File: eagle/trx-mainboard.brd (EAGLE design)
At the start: 94.8 x 82.9 mm, 0 parts

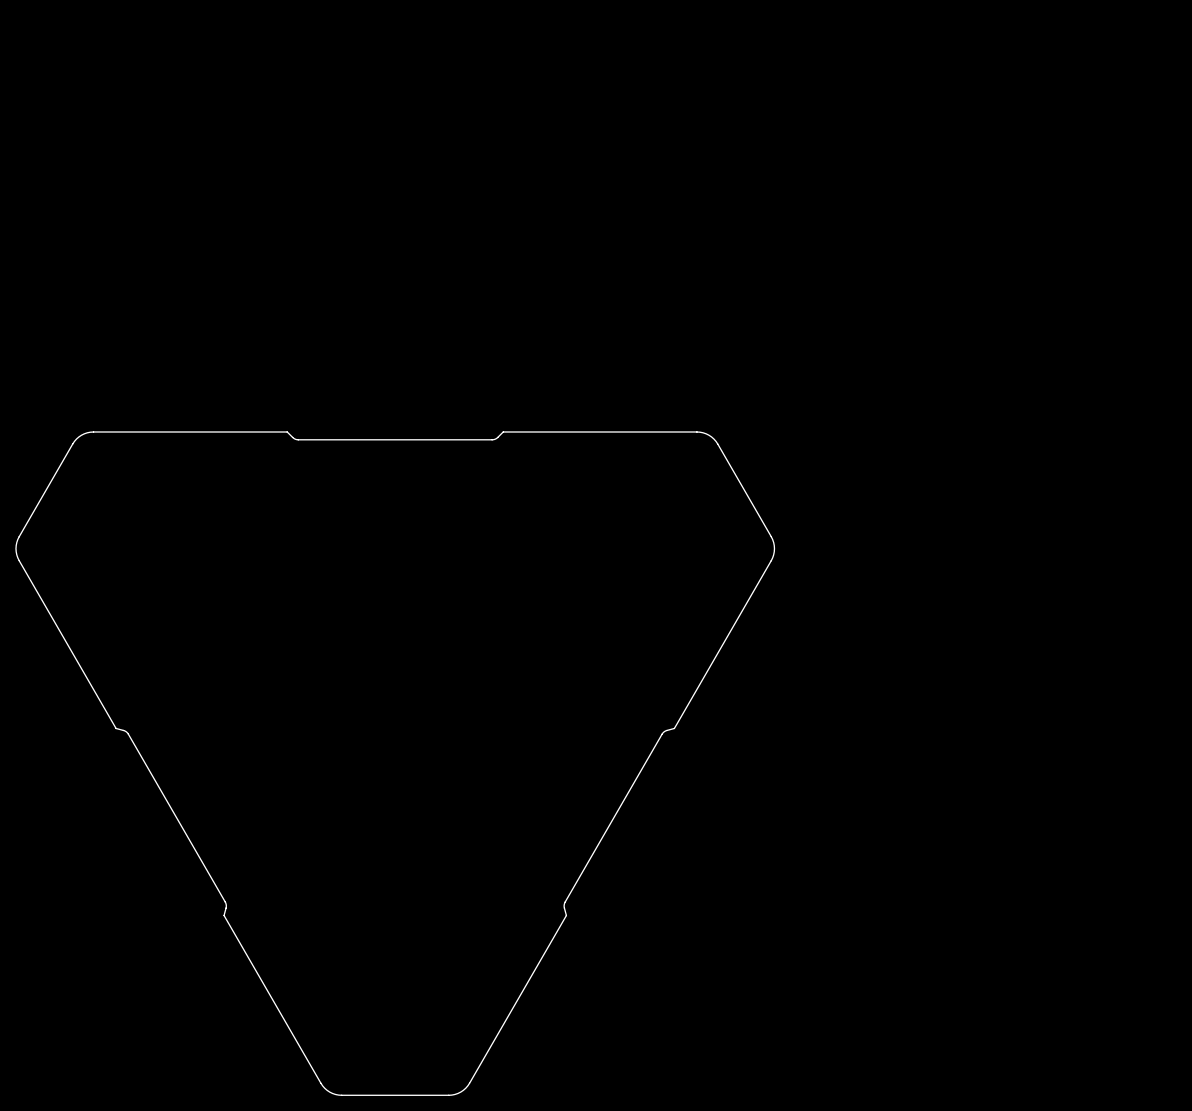
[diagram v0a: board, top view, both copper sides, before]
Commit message: Added eagle files and gitignore
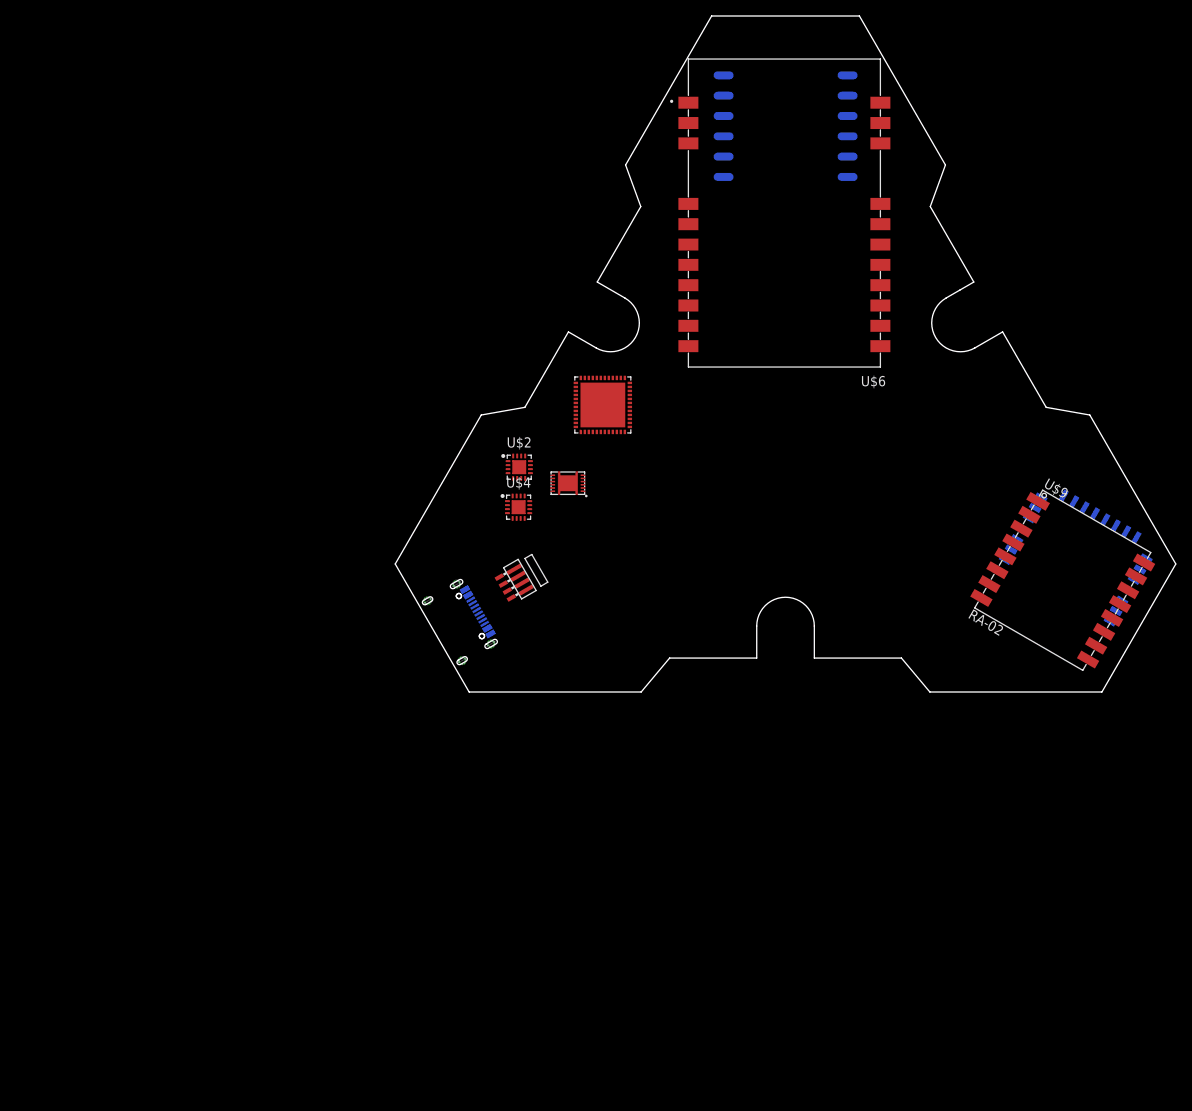
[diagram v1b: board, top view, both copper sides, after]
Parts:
- added J1: 629722000214, Wurth_Connectors_WR-USB:629722000214
- added U$1: L86-M33, quectel:L86-M33
- added U$10: STM32-F042X4/6-48, st-microelectronics:UFQFPN48-7X7
- added U$2: TPS6214X, texas-instruments:VQFN16-3X3
- added U$3: BQ27441, texas-instruments:SON12
- added U$4: BQ2407X, texas-instruments:VQFN16-3X3
- added U$5: JDY-23, bluetooth:JDY-23
- added U$6: E22-900M30S, ebyte:E22-900M30S
- added U$7: BC034-04-A-V-0150-L-C, con-gct:P-1X4/90-1.00X1.50MM-SMT
- added U$8: BC075-04-A-L-A, con-gct:S-1X4/90-1.00MM-SMT
- added U$9: RA-02, ai-thinker:RA-01/RA-02
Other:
- board size 94.8 x 82.9 mm -> 97.6 x 84.5 mm

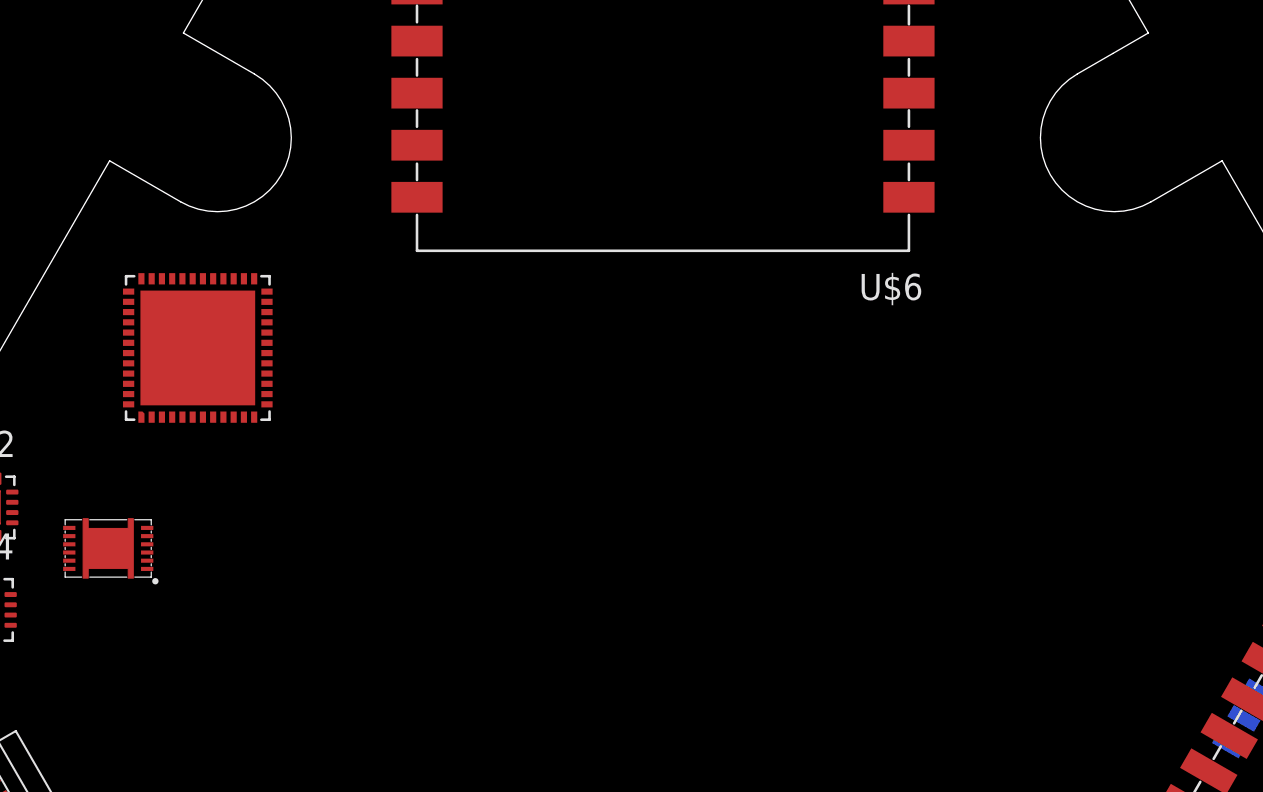
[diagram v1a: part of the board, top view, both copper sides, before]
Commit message: Added display pinheader
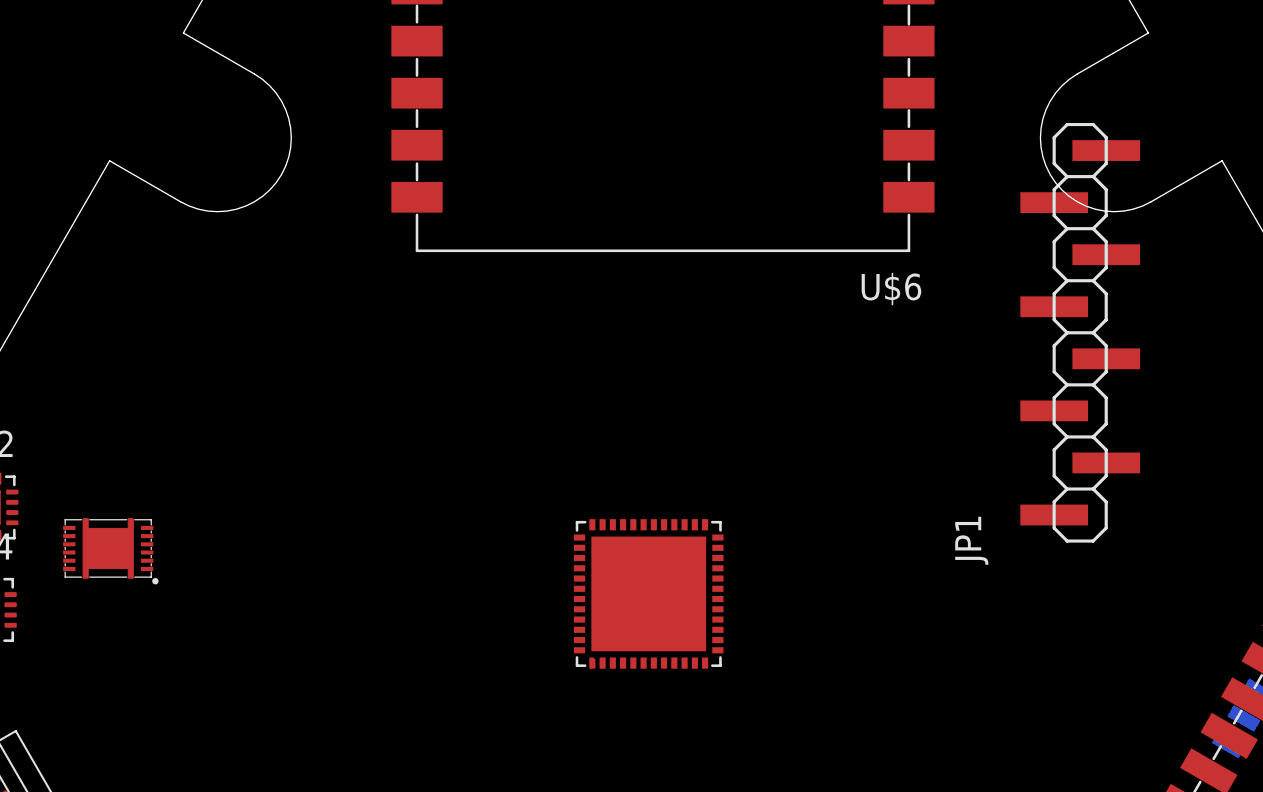
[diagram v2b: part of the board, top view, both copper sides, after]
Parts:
- added JP1: (no value), pinhead2:1X08SMD
- moved U$10 25.1 mm to (48.0, 23.9)
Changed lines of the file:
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@@
 </layers>
 <board>
+<fusionsync huburn="a.cGVyc29uYWw6dWUyZDQ3YTFj" projecturn="a.cGVyc29uYWw6dWUyZDQ3YTFjIzIwMTkxMDEyMjI1OTkyMjA2" f3durn="urn:adsk.wipprod:dm.lineage:G3ybIRbiT7ecl5LWR0nKqA" pcbguid="" lastpulledtime="" lastsyncedchangeguid="" latestrevisionid="6f82d806-30c5-4c96-a74c-11b18f3c1102" lastsyncedrevisionid="6f82d806-30c5-4c96-a74c-11b18f3c1102" lastboardhashguid="7c8f62d4-8a94-028a-21ff-13d31bc08e46" lastpushedtime="2023-05-01T20:54:56Z" linktopcb3d="true"/>
 <plain>
 <dimension x1="48" y1="40" x2="49" y2="5" x3="111.0774875" y3="24.287928125" textsize="1.778" layer="16"/>
@@
 <attribute name="VALUE" x="71.511796875" y="9.309734375" size="1.27" layer="21" rot="R330"/>
 </element>
-<element name="U$10" library="st-microelectronics" library_urn="urn:adsk.eagle:library:18661622" package="UFQFPN48-7X7" package3d_urn="urn:adsk.eagle:package:18661624/3" value="STM32-F042X4/6-48" x="25.95" y="35.88" smashed="yes" rot="R90"/>
+<element name="U$10" library="st-microelectronics" library_urn="urn:adsk.eagle:library:18661622" package="UFQFPN48-7X7" package3d_urn="urn:adsk.eagle:package:18661624/3" value="STM32-F042X4/6-48" x="47.95" y="23.88" smashed="yes" rot="R90"/>
+<element name="JP1" library="pinhead2" library_urn="urn:adsk.eagle:library:40219860" package="1X08SMD" package3d_urn="urn:adsk.eagle:package:40220540/2" value="" x="69" y="29" smashed="yes" rot="R90">
+<attribute name="NAME" x="64.1712" y="25.3838" size="1.27" layer="25" ratio="10" rot="R90"/>
+<attribute name="VALUE" x="72.175" y="26.46" size="1.27" layer="27" rot="R90"/>
+</element>
 </elements>
 <signals>
@@
 </note>
 <note version="8.3" severity="warning">
+Since Version 8.3, EAGLE supports Fusion synchronisation.
+This feature will not be available in this version and saving
+the document will break the link to the Fusion PCB feature.
+</note>
+<note version="8.3" severity="warning">

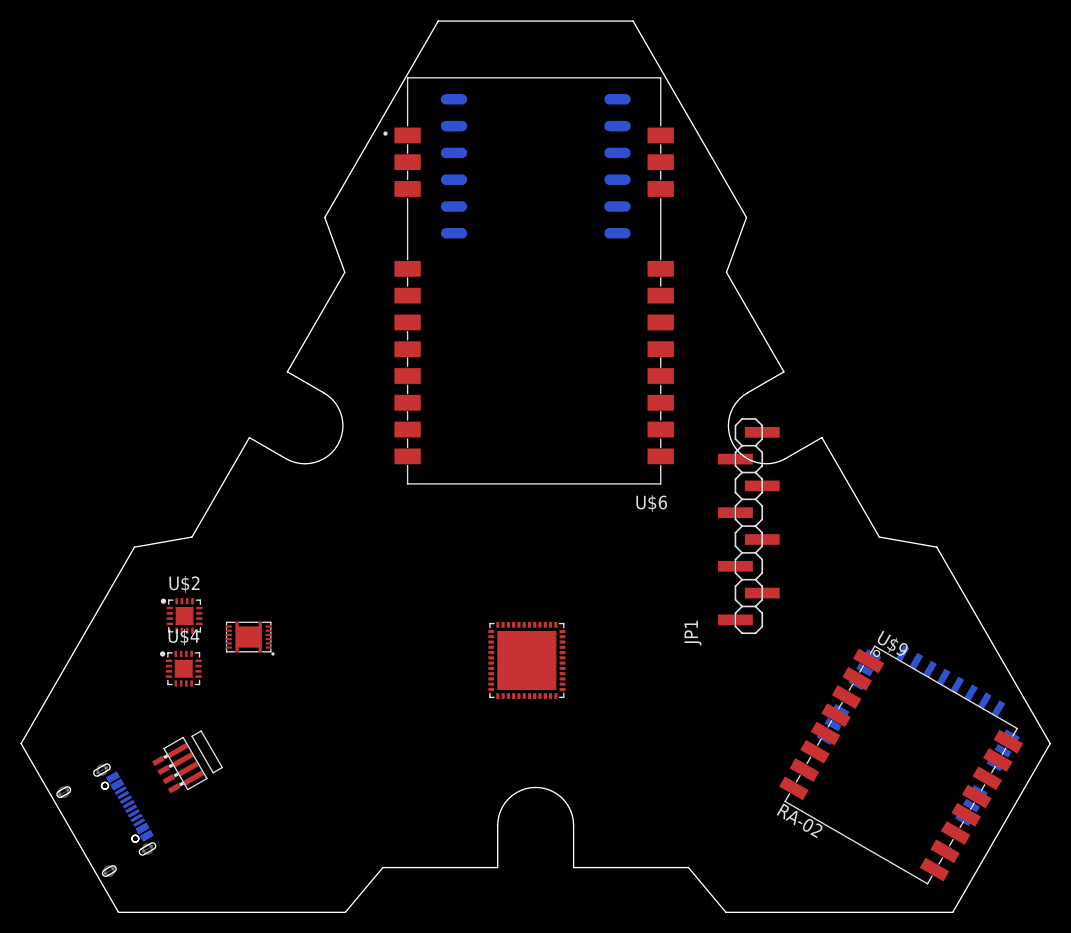
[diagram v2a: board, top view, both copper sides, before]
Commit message: Changed board layout
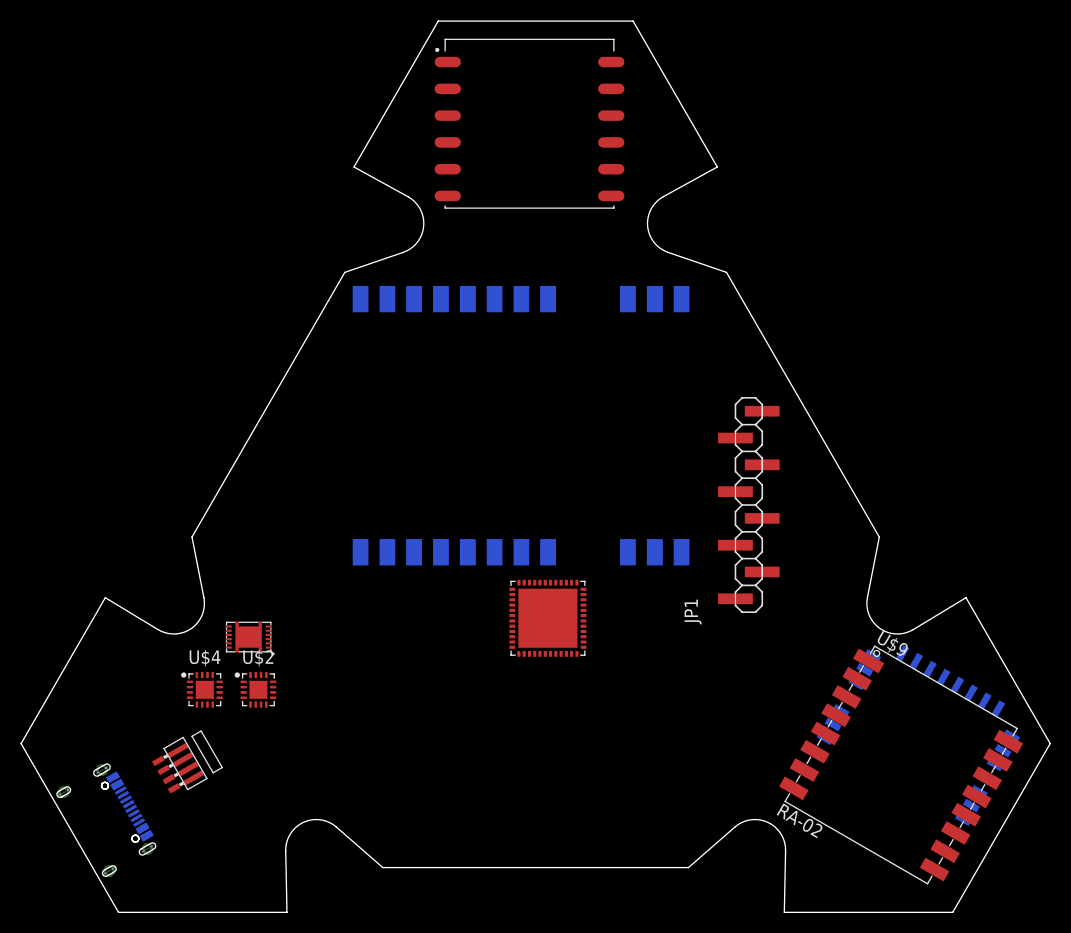
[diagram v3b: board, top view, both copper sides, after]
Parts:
- moved U$6 13.7 mm to (48.8, 46.1), flipped to the bottom, turned to 270 degrees
- moved U$2 9.90 mm to (22.5, 21.1)
- moved U$10 4.47 mm to (50.0, 27.9)
- moved U$1 3.58 mm to (48.2, 74.3), flipped to the top, turned to 0 degrees
- moved U$4 2.83 mm to (17.4, 21.1)
- moved JP1 2.00 mm to (69.0, 31.0)
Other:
- outline, holes or cut-outs redrawn

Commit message: Added further components to pcb
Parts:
- added C1, C11, C12, C13, C2, C3: 100nF, rcl:C0805
- added C10, C4, C5, C6, C8: 4.7uF, rcl:C0805
- added C7: 1uF, rcl:C0805
- added C9: (no value), rcl:PANASONIC_C
- added R1, R2: 5.1k, rcl:R0805
- added R3, R4, R5, R6: 3k, rcl:R0805
- U$3: value BQ27441 -> BQ2407X; device texas-instruments:SON12 -> texas-instruments:VQFN16-3X3
- U$4: value BQ2407X -> IHLP-1212; device texas-instruments:VQFN16-3X3 -> inductor-vishay:1212BZ
- U$6: value E22-900M30S -> E32-900M30S; device ebyte:E22-900M30S -> ebyte:E32-900M30S
- moved U$2 6.92 mm to (22.0, 28.0)
- moved U$3 4.89 mm to (26.0, 24.0), turned to 0 degrees
- moved U$4 4.61 mm to (21.0, 24.0)
- moved U$7 2.24 mm to (15.6, 14.2)
- moved U$8 1.68 mm to (17.0, 15.0), turned to 300 degrees
- moved U$1 0.20 mm to (48.4, 74.3)
- moved U$6 0.16 mm to (48.8, 46.3), turned to 90 degrees
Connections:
- new net +3V3: C1.1, C10.1, C13.1, C2.1, C3.1, C4.1, C8.1, C9.+, R6.1, U$10.24, U$10.48, U$10.9, U$2.14, U$4.2, U$6.10, U$6.9, U$9.3
- new net BT_RX: U$10.12
- new net BT_TX: U$10.13
- new net GND: C1.2, C10.2, C11.2, C12.2, C13.2, C2.2, C3.2, C4.2, C5.2, C6.2, C7.2, C8.2, C9.-, R3.1, R4.1, R5.2, U$10.23, U$10.35, U$10.47, U$10.8, U$2.7, U$2.8, U$3.14, U$3.15, U$3.17, U$3.4, U$3.5, U$3.8, U$6.1, U$6.11, U$6.12, U$6.17, U$6.18, U$6.2, U$6.26, U$6.28, U$6.3, U$6.4, U$6.5, U$8.1, U$9.1, U$9.16, U$9.2, U$9.9
- new net GPS_RX: U$10.30
- new net GPS_TX: U$10.31
- new net LORA1_D0: U$10.38, U$9.5
- new net LORA1_MISO: U$10.16, U$9.13
- new net LORA1_MOSI: U$10.17, U$9.14
- new net LORA1_RST: U$10.14, U$9.4
- new net LORA1_SCK: U$10.15, U$9.12
- new net LORA1_SSEL: U$10.29, U$9.15
- new net LORA2_D0: U$10.22, U$6.20
- new net LORA2_MISO: U$10.27, U$6.22
- new net LORA2_MOSI: U$10.28, U$6.23
- new net LORA2_RST: U$10.25, U$6.21
- new net LORA2_RXEN: U$10.46, U$6.6
- new net LORA2_SCK: U$10.21, U$6.24
- new net LORA2_SSEL: U$10.26, U$6.25
- new net LORA2_TXEN: U$10.45, U$6.7
- new net N$1: J1.A5, R2.2
- new net N$10: U$2.15, U$2.16, U$2.17, U$2.5, U$2.6
- new net N$2: J1.B5, R1.2
- new net N$3: R3.2, U$3.12
- new net N$4: R4.2, U$3.16
- new net N$5: R5.1, U$3.1
- new net N$6: U$2.1, U$2.2, U$2.3, U$4.1
- new net N$7: C12.1, U$2.9
- new net N$8: R6.2, U$2.4
- new net SWCLK: U$10.37
- new net SWDIO: U$10.34
- new net USB_D+: J1.A6, J1.B6, U$7.3
- new net USB_D-: J1.A7, J1.B7, U$7.2
- new net USB_DM: U$10.32, U$8.2
- new net USB_DP: U$10.33, U$8.3
- new net USB_GND: J1.A1, J1.A12, J1.B1, J1.B12, J1.S1, J1.S2, J1.S3, J1.S4, R1.1, R2.1, U$7.1
- new net USB_V: J1.A4, J1.A9, J1.B4, J1.B9, U$7.4
- new net V+: C11.1, C5.1, U$2.10, U$2.11, U$2.12, U$2.13, U$3.10, U$3.11, U$3.6
- new net VBAT+: C6.1, U$3.2, U$3.3
- new net VUSB: C7.1, U$3.13, U$8.4
